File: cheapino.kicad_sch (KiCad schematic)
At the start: 42 parts, among them K1 SW_Push, K10 SW_Push, K11 SW_Push, K12 SW_Push, K13 SW_Push, K14 SW_Push, K15 SW_Push, K16 SW_Push, K17 SW_Push, K18 SW_Push, K2 SW_Push, K3 SW_Push, K4 SW_Push, K5 SW_Push, K6 SW_Push, K7 SW_Push, K8 SW_Push, K9 SW_Push, U1 RP2040-Zero

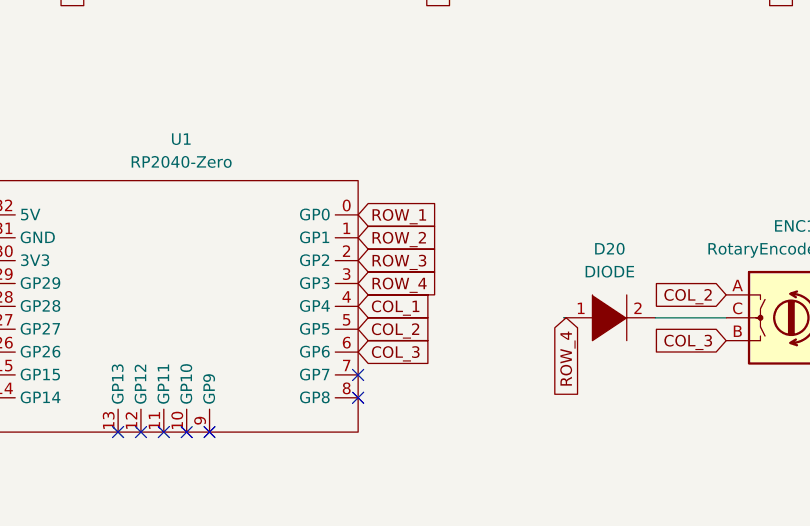
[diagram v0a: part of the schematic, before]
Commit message: passes drc
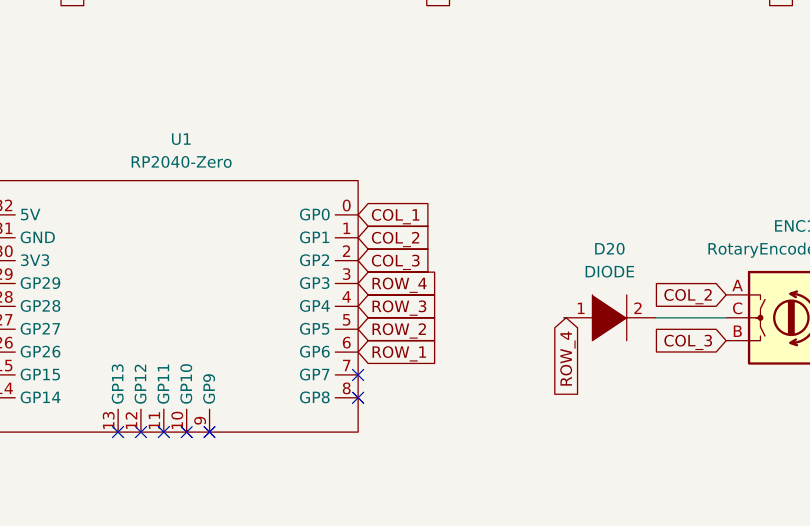
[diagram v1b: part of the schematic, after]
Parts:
- D1, D10, D11, D12, D13, D14, D15, D17, D18, D19, D2, D20, D3, D4, D5, D6, D7, D8, D9: footprint keyboard_parts:D_SOD123_axial -> keebio:Diode-dual
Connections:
- net COL_1: now also U1.0 (GP0); no longer U1.4 (GP4)
- net COL_2: now also U1.1 (GP1); no longer U1.5 (GP5)
- net COL_3: now also U1.2 (GP2); no longer U1.6 (GP6)
- net ROW_1: now also U1.6 (GP6); no longer U1.0 (GP0)
- net ROW_2: now also U1.5 (GP5); no longer U1.1 (GP1)
- net ROW_3: now also U1.4 (GP4); no longer U1.2 (GP2)

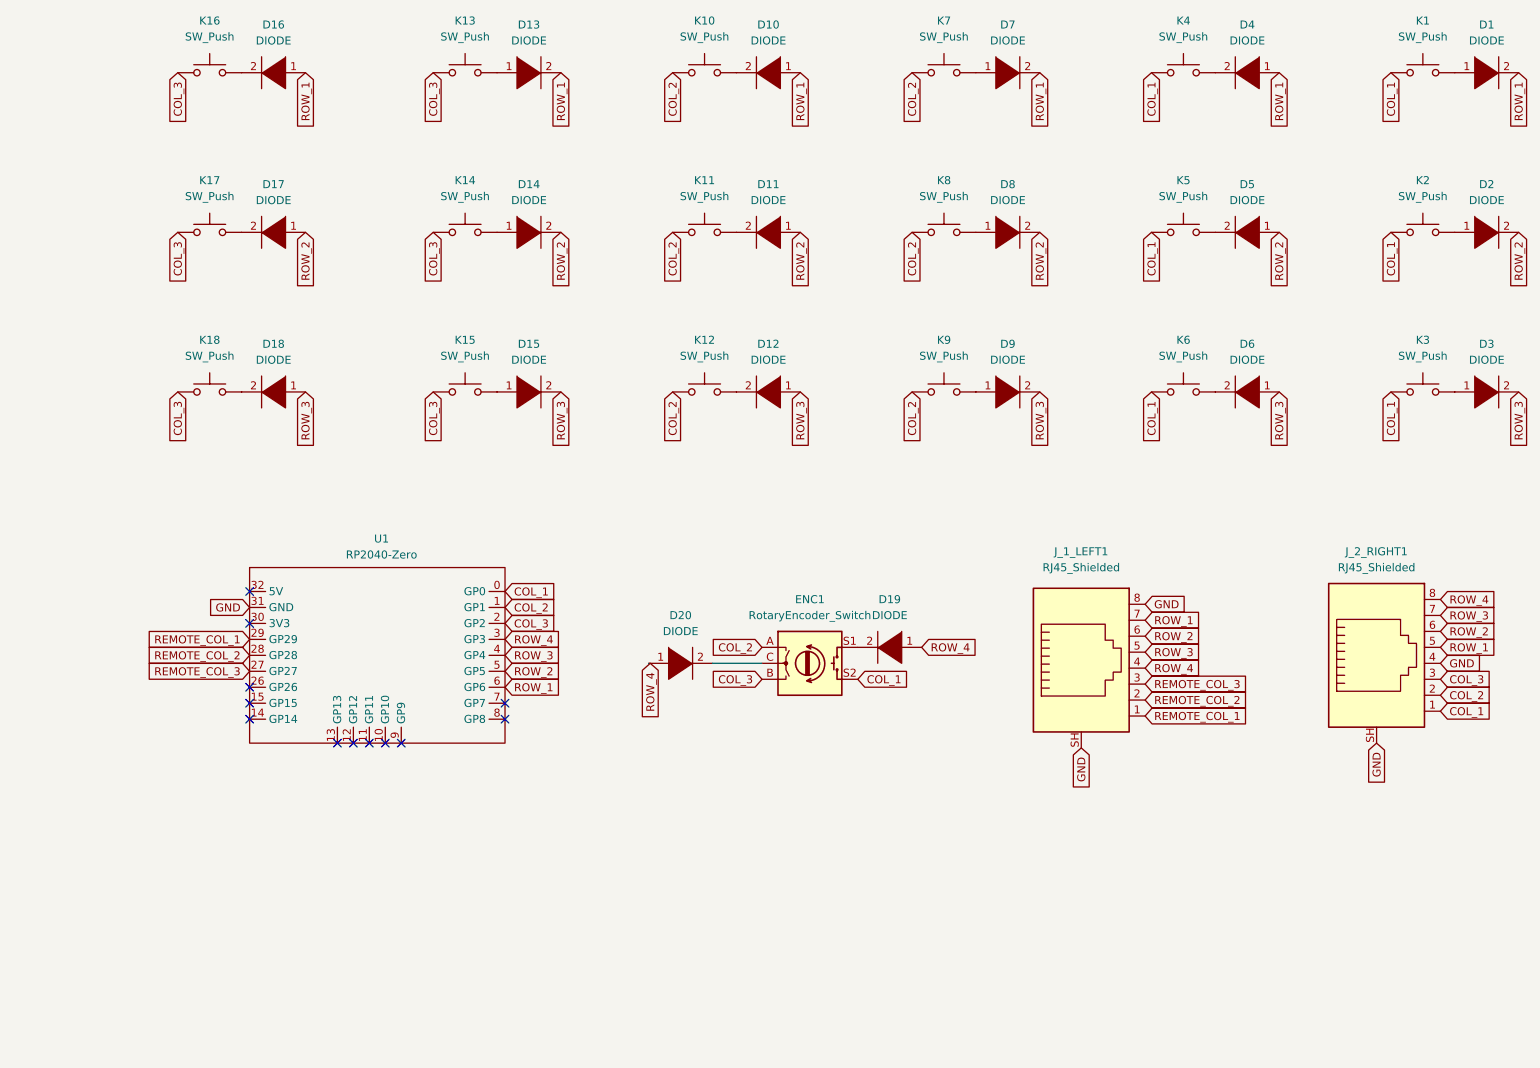
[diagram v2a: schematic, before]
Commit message: Hotswap support and solder jumpers
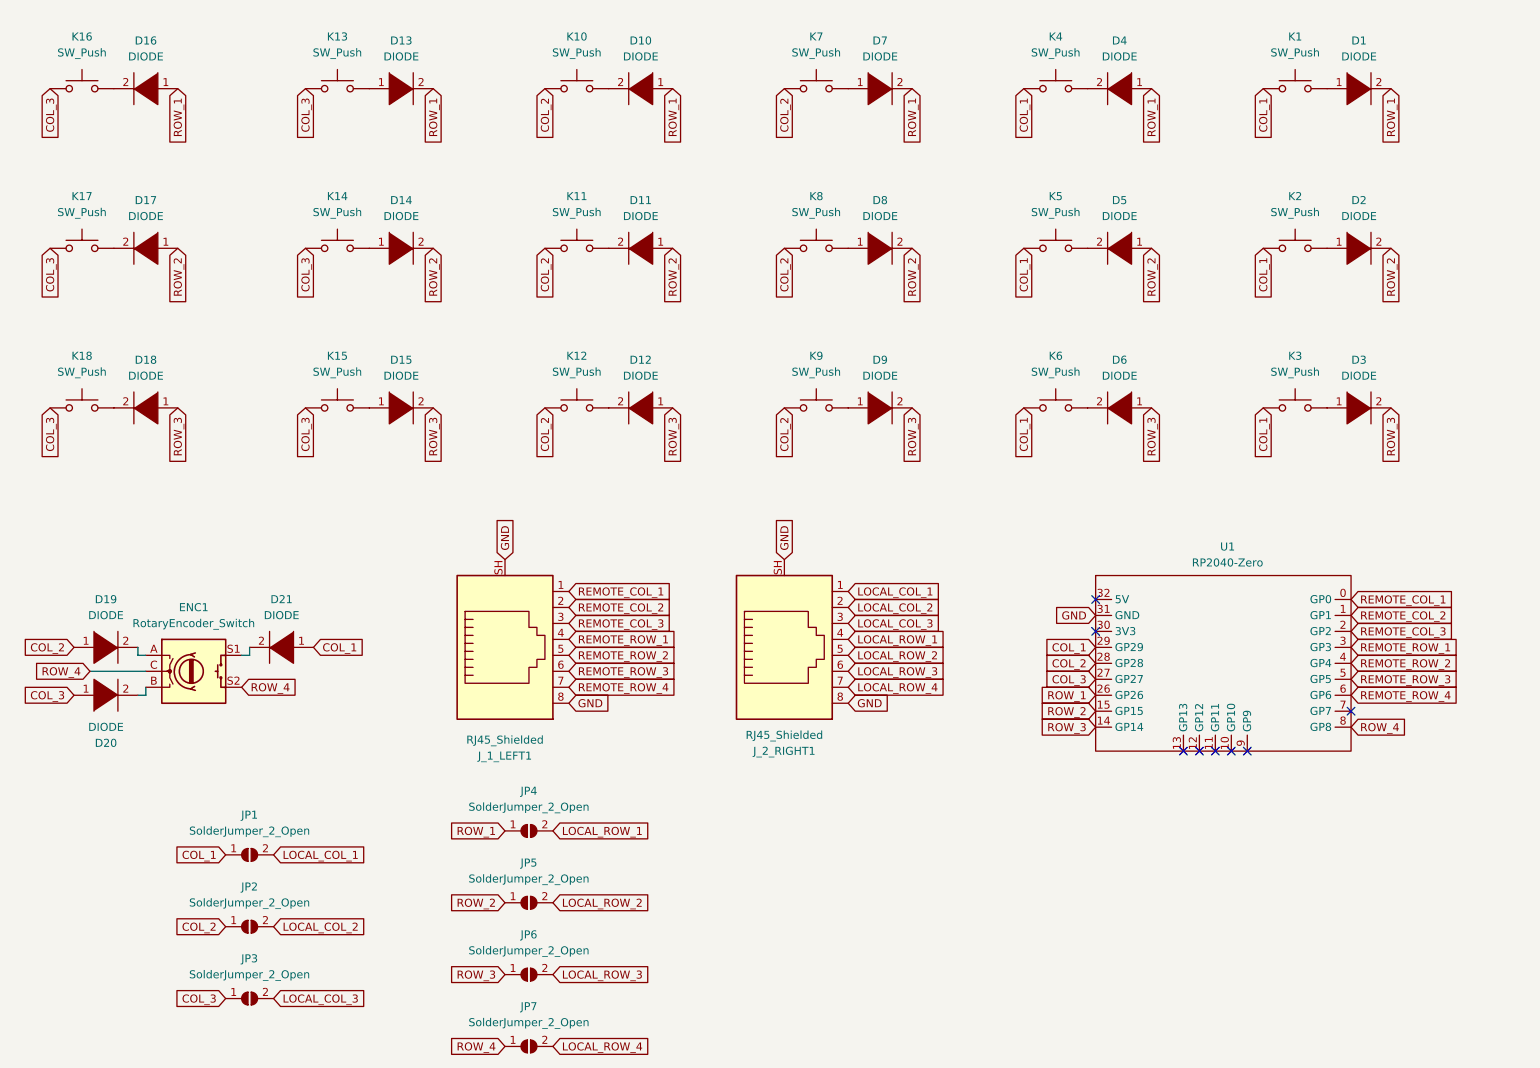
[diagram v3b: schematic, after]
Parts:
- added D21: DIODE, keebio:Diode-dual, symbol pspice:DIODE
- added JP1, JP2, JP3, JP4, JP5, JP6, JP7: SolderJumper_2_Open, Jumper:SolderJumper-2_P1.3mm_Open_TrianglePad1.0x1.5mm, symbol Jumper:SolderJumper_2_Open
- K1, K10, K11, K12, K13, K14, K15, K16, K17, K18, K2, K3, K4, K5, K6, K7, K8, K9: footprint project_footprints:SW_MX_reversible_minimal -> project_footprints:Kailh_socket_MX_optional_reversible
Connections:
- net COL_1: now also U1.29 (GP29), D21.1 (K), JP1.1 (A); no longer ENC1.S2, J_2_RIGHT1.1, U1.0 (GP0)
- net COL_2: now also D19.1 (K), U1.28 (GP28), JP2.1 (A); no longer ENC1.A, J_2_RIGHT1.2, U1.1 (GP1)
- net COL_3: now also D20.1 (K), U1.27 (GP27), JP3.1 (A); no longer ENC1.B, J_2_RIGHT1.3, U1.2 (GP2)
- net GND: now also J_2_RIGHT1.8; no longer J_2_RIGHT1.4
- net REMOTE_COL_1: now also U1.0 (GP0); no longer U1.29 (GP29)
- net REMOTE_COL_2: now also U1.1 (GP1); no longer U1.28 (GP28)
- net REMOTE_COL_3: now also U1.2 (GP2); no longer U1.27 (GP27)
- net ROW_1: now also U1.26 (GP26), JP4.1 (A); no longer J_1_LEFT1.7, J_2_RIGHT1.5, U1.6 (GP6)
- net ROW_2: now also U1.15 (GP15), JP5.1 (A); no longer J_1_LEFT1.6, J_2_RIGHT1.6, U1.5 (GP5)
- net ROW_3: now also U1.14 (GP14), JP6.1 (A); no longer J_1_LEFT1.5, J_2_RIGHT1.7, U1.4 (GP4)
- net ROW_4: now also ENC1.C, ENC1.S2, U1.8 (GP8), JP7.1 (A); no longer D19.1 (K), D20.1 (K), J_1_LEFT1.4, J_2_RIGHT1.8, U1.3 (GP3)
- net at D19.2 (A): now also ENC1.A; no longer ENC1.S1
- net at D20.2 (A): now also ENC1.B; no longer ENC1.C
- new net: D21.2 (A), ENC1.S1
- new net LOCAL_COL_1: JP1.2 (B), J_2_RIGHT1.1
- new net LOCAL_COL_2: JP2.2 (B), J_2_RIGHT1.2
- new net LOCAL_COL_3: JP3.2 (B), J_2_RIGHT1.3
- new net LOCAL_ROW_1: JP4.2 (B), J_2_RIGHT1.4
- new net LOCAL_ROW_2: JP5.2 (B), J_2_RIGHT1.5
- new net LOCAL_ROW_3: JP6.2 (B), J_2_RIGHT1.6
- new net LOCAL_ROW_4: JP7.2 (B), J_2_RIGHT1.7
- new net REMOTE_ROW_1: J_1_LEFT1.4, U1.3 (GP3)
- new net REMOTE_ROW_2: J_1_LEFT1.5, U1.4 (GP4)
- new net REMOTE_ROW_3: J_1_LEFT1.6, U1.5 (GP5)
- new net REMOTE_ROW_4: J_1_LEFT1.7, U1.6 (GP6)
- no-connect marks 12 -> 8
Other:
- moved on the sheet: D1, D10, D11, D12, D13, D14, D15, D16, D17, D18, D2, D3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

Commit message: V2 First draft
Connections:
- net COL_1: now also U1.14 (GP14); no longer U1.29 (GP29)
- net COL_2: now also U1.15 (GP15); no longer U1.28 (GP28)
- net COL_3: now also U1.26 (GP26); no longer U1.27 (GP27)
- net GND: now also J_1_LEFT1.1, J_2_RIGHT1.1; no longer J_1_LEFT1.8, J_2_RIGHT1.8
- net ROW_1: now also U1.27 (GP27); no longer U1.26 (GP26)
- net ROW_2: now also U1.28 (GP28); no longer U1.15 (GP15)
- net ROW_3: now also U1.29 (GP29); no longer U1.14 (GP14)
- net LOCAL_COL_1 renamed R_COL_1
- net R_COL_1: now also J_1_LEFT1.2, J_2_RIGHT1.8, U1.0 (GP0); no longer J_2_RIGHT1.1
- net LOCAL_COL_2 renamed R_COL_2
- net R_COL_2: now also J_1_LEFT1.3, J_2_RIGHT1.7, U1.1 (GP1); no longer J_2_RIGHT1.2
- net LOCAL_COL_3 renamed R_COL_3
- net R_COL_3: now also J_1_LEFT1.4, J_2_RIGHT1.6, U1.2 (GP2); no longer J_2_RIGHT1.3
- net LOCAL_ROW_1 renamed R_ROW_1
- net R_ROW_1: now also J_1_LEFT1.5, J_2_RIGHT1.5, U1.3 (GP3); no longer J_2_RIGHT1.4
- net LOCAL_ROW_2 renamed R_ROW_3
- net R_ROW_3: now also J_1_LEFT1.7, J_2_RIGHT1.3, U1.5 (GP5); no longer J_2_RIGHT1.5
- net LOCAL_ROW_3 renamed R_ROW_2
- net R_ROW_2: now also J_1_LEFT1.6, J_2_RIGHT1.4, U1.4 (GP4); no longer J_2_RIGHT1.6
- net LOCAL_ROW_4 renamed R_ROW_4
- net R_ROW_4: now also J_1_LEFT1.8, J_2_RIGHT1.2, U1.6 (GP6); no longer J_2_RIGHT1.7
- removed net REMOTE_COL_1: J_1_LEFT1.1, U1.0 (GP0)
- removed net REMOTE_COL_2: J_1_LEFT1.2, U1.1 (GP1)
- removed net REMOTE_COL_3: J_1_LEFT1.3, U1.2 (GP2)
- removed net REMOTE_ROW_1: J_1_LEFT1.4, U1.3 (GP3)
- removed net REMOTE_ROW_2: J_1_LEFT1.5, U1.4 (GP4)
- removed net REMOTE_ROW_3: J_1_LEFT1.6, U1.5 (GP5)
- removed net REMOTE_ROW_4: J_1_LEFT1.7, U1.6 (GP6)

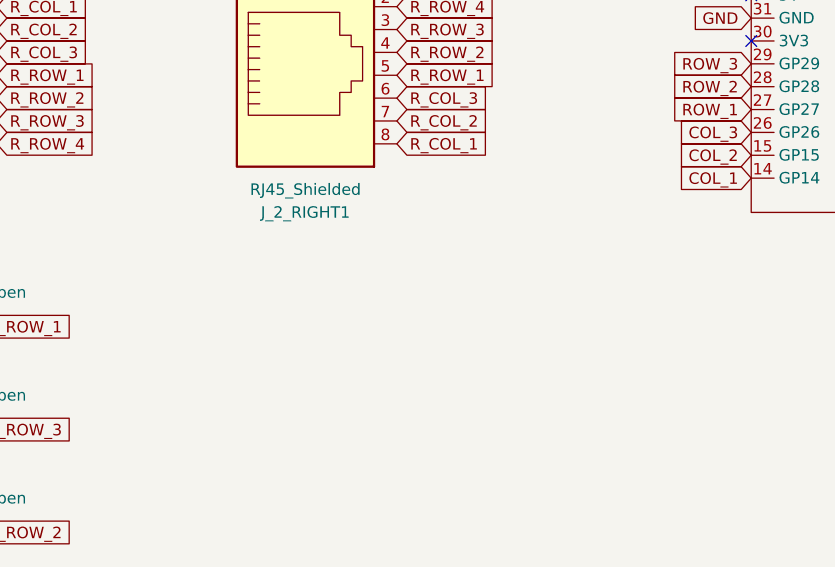
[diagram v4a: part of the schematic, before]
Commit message: Added logo copper layer, removed some labels
This commit was ordered from jlcpcb
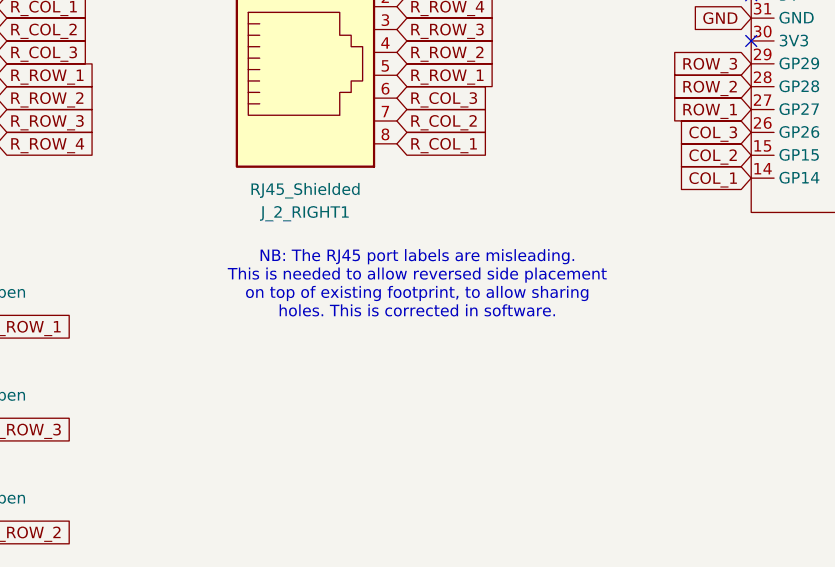
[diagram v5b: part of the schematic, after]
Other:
- note added: "NB: The RJ45 port labels are misleading. This is needed to allow reversed side placement on top of existing footprint, to allow sharing holes. This is corrected in software."
